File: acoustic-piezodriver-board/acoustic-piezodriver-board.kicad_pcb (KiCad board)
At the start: 4 copper layers, 100 x 62 mm, 161 parts, among them J301 Conn_02x06_Odd_Even, J501 Conn_02x06_Odd_Even, P101 WJ128V-5.0-3P, P201 WJ128V-5.0-3P, Q501 AO3400A, Q502 AO3400A, U10 NCE6005AS, U101 AMS1117-3.3, U102 TMCS1108A3UQDR, U201 UCC27282DR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

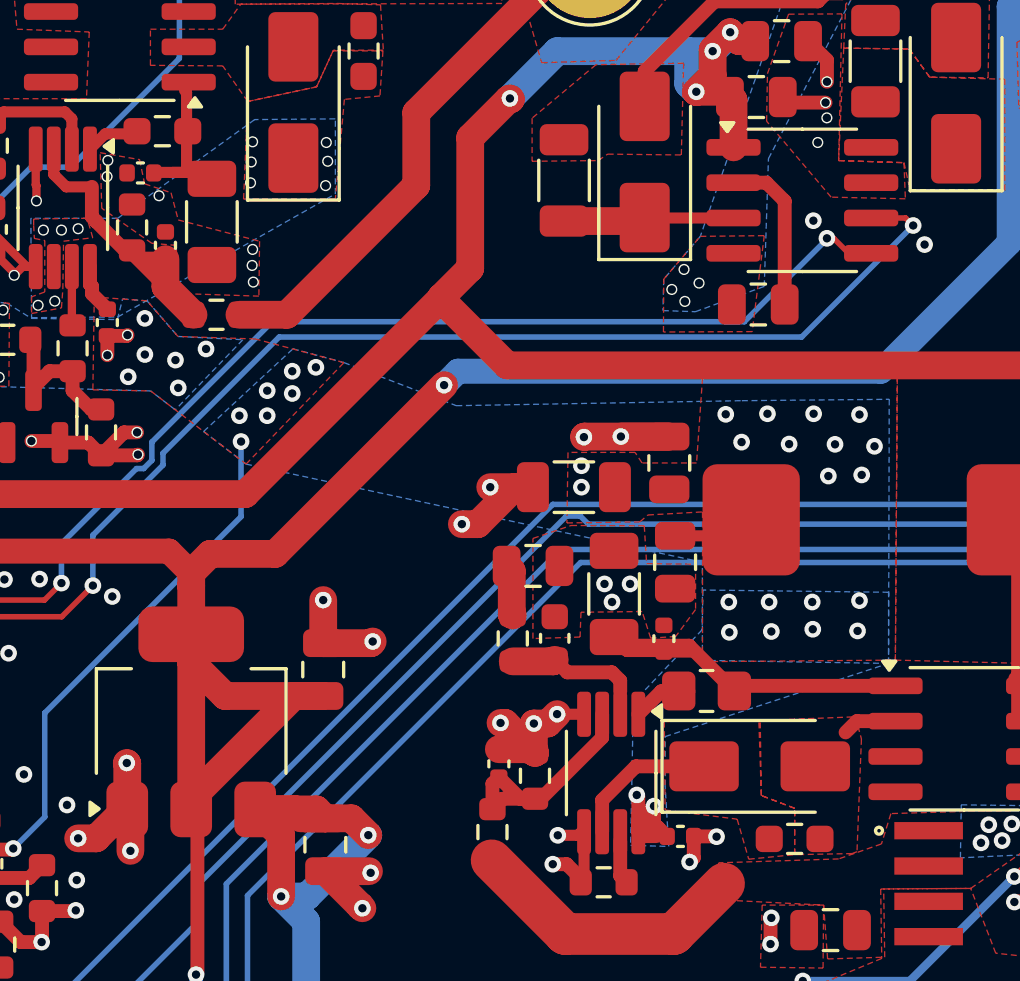
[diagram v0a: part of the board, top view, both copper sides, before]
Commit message: fixed erc and drc errors completely, added 3d models for connectors, finished DFM (next) create gerbers, check
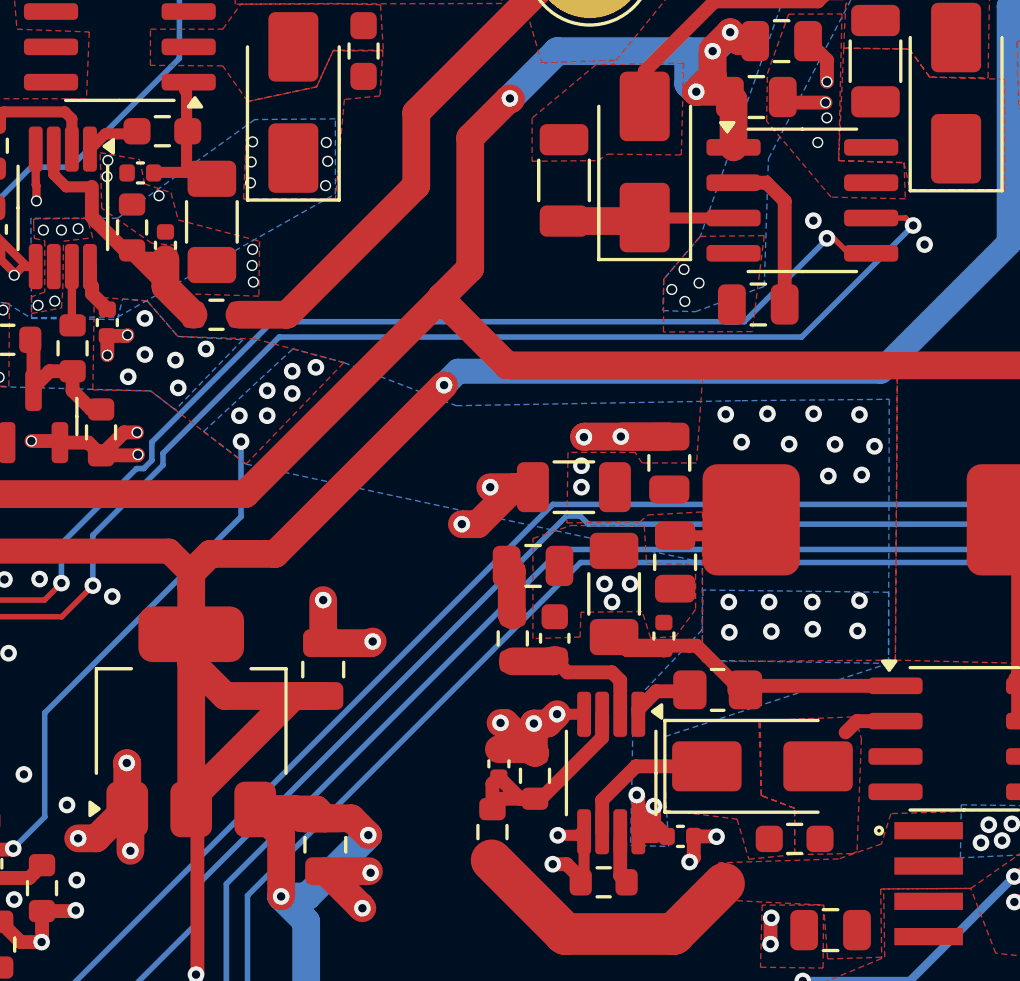
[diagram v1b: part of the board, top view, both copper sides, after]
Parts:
- moved R21 0.40 mm to (103.4, 124.2)
- moved D5 0.10 mm to (105.0, 126.9)
- moved C37 0.10 mm to (101.5, 122.2)
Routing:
- net Net-(U10B-S2): track 16.1 -> 14.2 mm
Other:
- board text added: "+10V"
- board text added: "+INV"
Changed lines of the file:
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@@
 		)
 		(embedded_fonts no)
-		(model "/WJ128V-5.0-3P.3dshapes/CONN-TH_3P-P5.00_WJ128V-5.0-3P.wrl"
+		(model " ${KISYS3DMOD}/TerminalBlock_Phoenix.3dshapes/TerminalBlock_Phoenix_MKDS-1,5-3_1x03_P5.00mm_Horizontal.wrl"
 			(offset
-				(xyz -0.3 -0.15 0)
+				(xyz 0 0.35 0)
 			)
 			(scale
@@
 			)
 			(rotate
-				(xyz 0 0 180)
+				(xyz -0 -0 -0)
+			)
+		)
+		(model "${KICAD9_3DMODEL_DIR}/TerminalBlock_Phoenix.3dshapes/TerminalBlock_Phoenix_MKDS-1,5-3-5.08_1x03_P5.08mm_Horizontal.wrl"
+			(offset
+				(xyz 5.25 0 0)
+			)
+			(scale
+				(xyz 1 1 1)
+			)
+			(rotate
+				(xyz -0 -0 180)
 			)
 		)
@@
 		)
 		(embedded_fonts no)
-		(model "/WJ128V-5.0-3P.3dshapes/CONN-TH_3P-P5.00_WJ128V-5.0-3P.wrl"
+		(model " ${KISYS3DMOD}/TerminalBlock_Phoenix.3dshapes/TerminalBlock_Phoenix_MKDS-1,5-3_1x03_P5.00mm_Horizontal.wrl"
 			(offset
-				(xyz -0.3 -0.15 0)
+				(xyz 0 0.35 0)
 			)
 			(scale
@@
 			)
 			(rotate
-				(xyz 0 0 180)
+				(xyz -0 -0 -0)
+			)
+		)
+		(model "${KICAD9_3DMODEL_DIR}/TerminalBlock_Phoenix.3dshapes/TerminalBlock_Phoenix_MKDS-1,5-3-5.08_1x03_P5.08mm_Horizontal.wrl"
+			(offset
+				(xyz 5.25 0 0)
+			)
+			(scale
+				(xyz 1 1 1)
+			)
+			(rotate
+				(xyz -0 -0 180)
 			)
 		)
@@
 	(footprint "Capacitor_SMD:C_0402_1005Metric"
 		(layer "F.Cu")
-		(at 101.465 122.32 90)
+		(at 101.465 122.22 90)
 		(descr "Capacitor SMD 0402 (1005 Metric), square (rectangular) end terminal, IPC-7351 nominal, (Body size source: IPC-SM-782 page 76, https://www.pcb-3d.com/wordpress/wp-content/uploads/ipc-sm-782a_amendment_1_and_2.pdf), generated with kicad-footprint-generator")
 		(tags "capacitor")
@@
 	(footprint "Diode_SMD:D_SMA"
 		(layer "F.Cu")
-		(at 104.91 126.91)
+		(at 105.01 126.91)
 		(descr "Diode SMA (DO-214AC)")
 		(tags "Diode SMA (DO-214AC)")
@@
 			)
 		)
+		(property "LCSC Part Number" "C2867844"
+			(at 0 0 0)
+			(unlocked yes)
+			(layer "F.Fab")
+			(hide yes)
+			(effects
+				(font
+					(size 1 1)
+					(thickness 0.15)
+				)
+			)
+		)
 		(sheetname "/INVERTER/")
 		(sheetfile "inverter.kicad_sch")
@@
 	(footprint "Resistor_SMD:R_0805_2012Metric_Pad1.20x1.40mm_HandSolder"
 		(layer "F.Cu")
-		(at 103 124.2)
+		(at 103.4 124.16)
 		(descr "Resistor SMD 0805 (2012 Metric), square (rectangular) end terminal, IPC-7351 nominal with elongated pad for handsoldering. (Body size source: IPC-SM-782 page 72, https://www.pcb-3d.com/wordpress/wp-content/uploads/ipc-sm-782a_amendment_1_and_2.pdf), generated with kicad-footprint-generator")
 		(tags "resistor handsolder")
@@
 			)
 		)
+		(property "LCSC Part Number" "C2867844"
+			(at 0 0 0)
+			(unlocked yes)
+			(layer "F.Fab")
+			(hide yes)
+			(effects
+				(font
+					(size 1 1)
+					(thickness 0.15)
+				)
+			)
+		)
 		(sheetname "/INVERTER/")
 		(sheetfile "inverter.kicad_sch")
@@
 		(layer "Edge.Cuts")
 	)
+	(gr_text "+10V"
+		(at 56.31 126.85 0)
+		(layer "B.SilkS")
+		(effects
+			(font
+				(size 1.5 1.5)
+				(thickness 0.2)
+				(bold yes)
+			)
+			(justify left bottom mirror)
+		)
+	)
+	(gr_text "+INV"
+		(at 97.33 101.8 0)
+		(layer "B.SilkS")
+		(effects
+			(font
+				(size 1.5 1.5)
+				(thickness 0.2)
+				(bold yes)
+			)
+			(justify left bottom mirror)
+		)
+	)
 	(segment
 		(start 107.585 98.407736)
@@
 	)
 	(segment
+		(start 102.371 122.571)
+		(end 101.694 122.571)
+		(width 0.4)
+		(layer "F.Cu")
+		(net 16)
+	)
+	(segment
 		(start 99.675 122.26)
 		(end 99.986 122.571)
@@
 	)
 	(segment
-		(start 102.371 122.571)
-		(end 104 124.2)
+		(start 100.145 122.73)
+		(end 101.5 122.73)
 		(width 0.5)
 		(layer "F.Cu")
@@
 	)
 	(segment
-		(start 104 124.2)
-		(end 102.6 122.8)
+		(start 101.694 122.571)
+		(end 101.465 122.8)
 		(width 0.4)
 		(layer "F.Cu")
@@
 	)
 	(segment
-		(start 100.145 122.73)
-		(end 101.5 122.73)
+		(start 99.986 122.571)
+		(end 102.371 122.571)
 		(width 0.5)
 		(layer "F.Cu")
@@
 	)
 	(segment
-		(start 99.986 122.571)
-		(end 102.371 122.571)
+		(start 102.641 122.571)
+		(end 104 123.93)
+		(width 0.5)
+		(layer "F.Cu")
+		(net 16)
+	)
+	(segment
+		(start 104 123.93)
+		(end 104 124.2)
+		(width 0.5)
+		(layer "F.Cu")
+		(net 16)
+	)
+	(segment
+		(start 102.371 122.571)
+		(end 102.641 122.571)
 		(width 0.5)
 		(layer "F.Cu")
@@
 	)
 	(segment
-		(start 102.6 122.8)
-		(end 101.465 122.8)
-		(width 0.4)
-		(layer "F.Cu")
-		(net 16)
-	)
-	(segment
 		(start 114.205 123.85)
 		(end 114.205 118.145)
@@
 	)
 	(segment
-		(start 84.25 105.55)
-		(end 83.79 105.55)
-		(width 0.4)
-		(layer "F.Cu")
-		(net 29)
-	)
-	(segment
 		(start 84.23 102.61)
 		(end 84.3 102.68)
@@
 	)
 	(segment
-		(start 101.3725 124.21)
+		(start 102.35 124.21)
+		(end 101.19 124.21)
+		(width 0.5)
+		(layer "F.Cu")
+		(net 61)
+	)
+	(segment
+		(start 100.545 124.855)
 		(end 100.545 125.0375)
 		(width 0.5)
@@
 	)
 	(segment
-		(start 102.35 124.21)
-		(end 101.3725 124.21)
+		(start 101.19 124.21)
+		(end 100.545 124.855)
 		(width 0.5)
 		(layer "F.Cu")

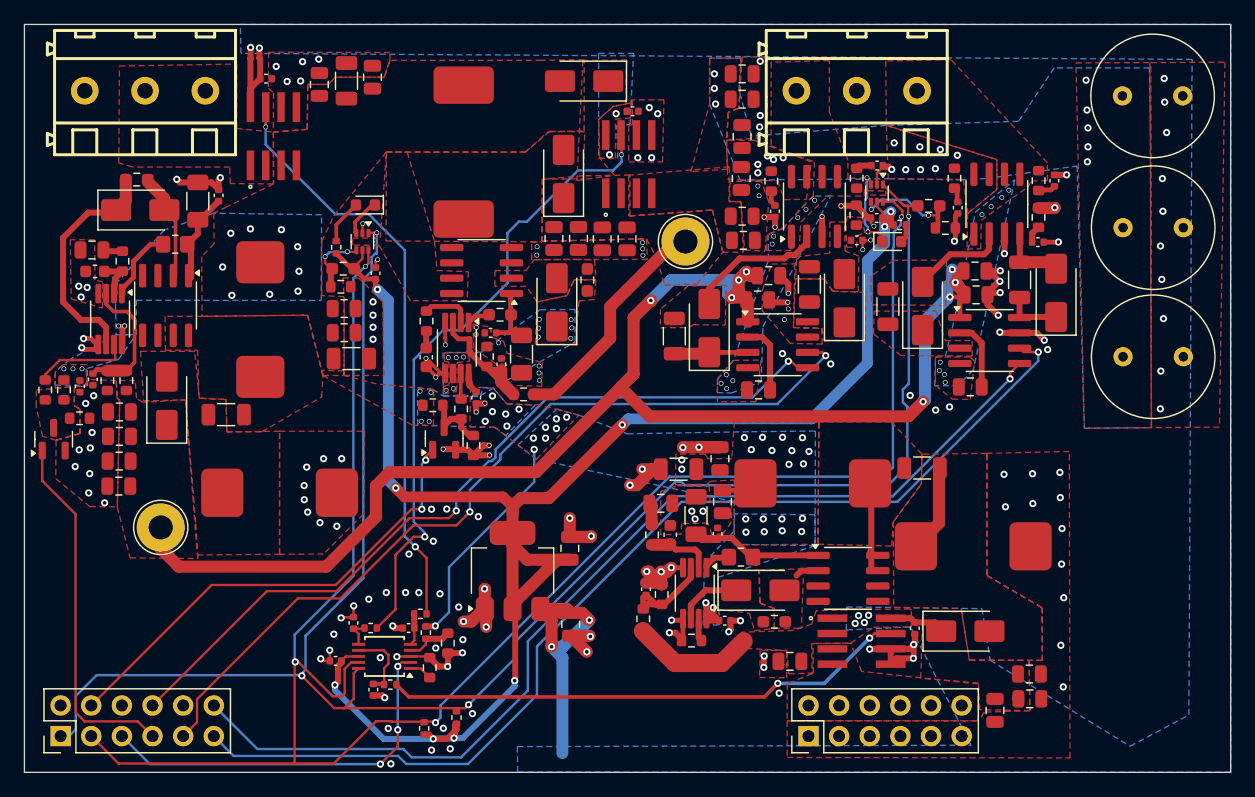
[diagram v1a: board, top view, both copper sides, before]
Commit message: added testpoints on fb and isense pins (next) double-check schematic and order
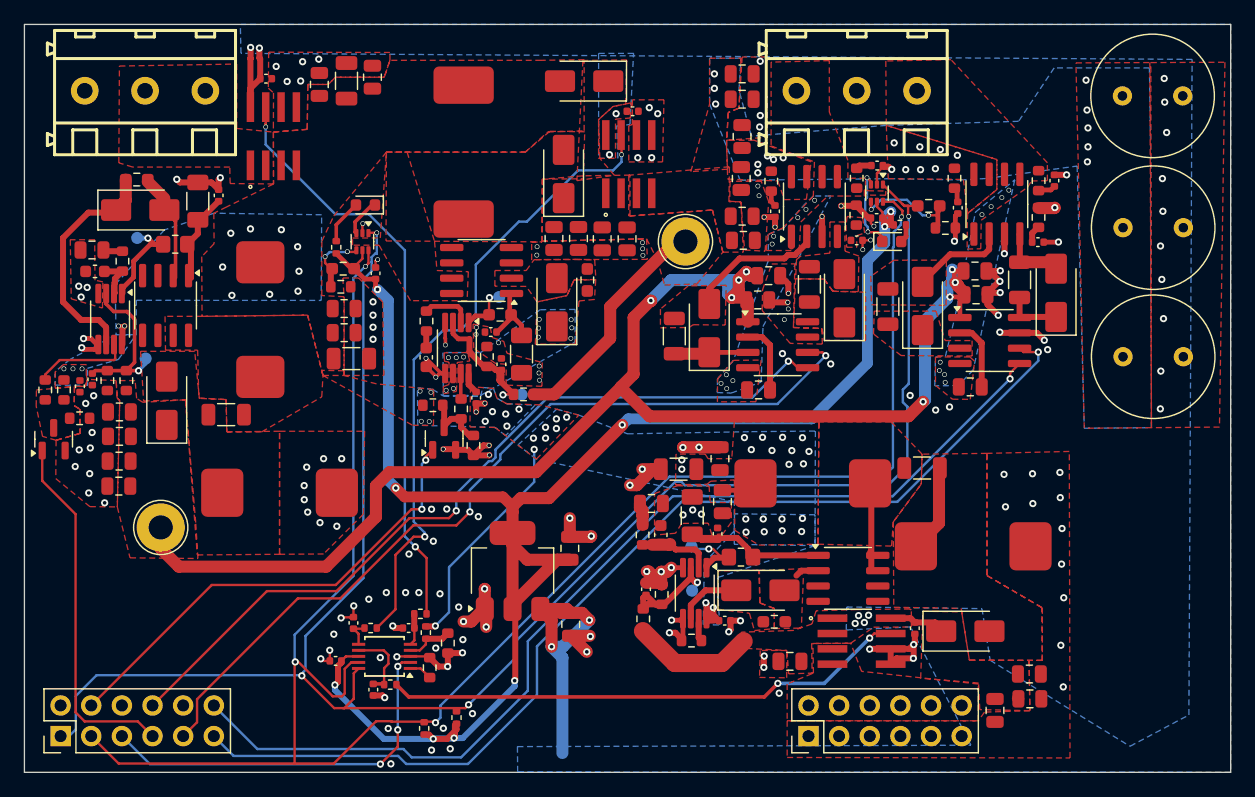
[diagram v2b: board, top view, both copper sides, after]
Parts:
- added TP301: TestPoint, TestPoint:TestPoint_Pad_D1.0mm, B.Cu at (99.3, 126.9)
- added TP302: Testpoint, TestPoint:TestPoint_Pad_D1.0mm, B.Cu at (99.3, 123.3)
- added TP503: Testpoint, TestPoint:TestPoint_Pad_D1.0mm, B.Cu at (53.4, 97.7)
- added TP504: TestPoint, TestPoint:TestPoint_Pad_D1.0mm, B.Cu at (54.0, 107.7)
- added TP505: TestPoint, TestPoint:TestPoint_Pad_D1.0mm, B.Cu at (83.4, 102.6)
- added TP506: TestPoint, TestPoint:TestPoint_Pad_D1.0mm, B.Cu at (85.2, 110.7)
- moved C32 0.78 mm to (96.0, 119.7)
- moved C33 0.78 mm to (96.8, 122.3)
- moved R19 0.78 mm to (95.2, 122.3)
- moved R22 0.32 mm to (99.4, 120.7)
- moved C521 0.07 mm to (82.7, 105.5)
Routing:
- net Net-(U9-I_{SEN}): track 2.25 -> 5.72 mm, vias 0 -> 1
- net Net-(U502-FB): track 11.2 -> 13.8 mm, vias 0 -> 1
- net Net-(U504-I_{SEN}): track 1.92 -> 4.34 mm, vias 0 -> 1
- net Net-(U502-I_{SEN}): track 6.08 -> 8.32 mm, vias 0 -> 1
- net Net-(U9-FB): track 8.72 -> 10.4 mm, vias 0 -> 1
- net Net-(U504-FB): track 11.0 -> 12.7 mm, vias 0 -> 1
- net Net-(U503B-S2): track 5.14 -> 5.93 mm
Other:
- board text added: "10V SEPIC"
- board text added: "40V BOOST"
- board text added: "6V SEPIC"
- board text added: "FB"
- board text added: "ISEN"

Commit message: added gerbers
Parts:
- added FID101: Fiducial, Fiducial:Fiducial_1mm_Mask2mm, F.Cu at (127.8, 86.1)
- added FID102: Fiducial, Fiducial:Fiducial_1mm_Mask2mm, F.Cu at (48.6, 93.3)
- added FID103: Fiducial, Fiducial:Fiducial_1mm_Mask2mm, F.Cu at (136.8, 128.7)
- added FID104: Fiducial, Fiducial:Fiducial_1mm_Mask2mm, F.Cu at (51.0, 130.8)
- added H101: MountingHole, MountingHole:ToolingHole_1.152mm, F.Cu at (125.7, 85.1)
- added H102: MountingHole, MountingHole:ToolingHole_1.152mm, F.Cu at (136.6, 131.4)
- added H103: MountingHole, MountingHole:ToolingHole_1.152mm, F.Cu at (50.7, 128.6)
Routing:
- net /SENSORS_CONN/T_SDA: track 155.8 -> 155.1 mm
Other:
- board text added: "PCONN 5V"
- board text added: "PCONN IN"
- board text added: "PCONN INV"
- board text added: "SIGCON"
